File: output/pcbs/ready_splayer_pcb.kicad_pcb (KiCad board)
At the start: 2 copper layers, 124.4 x 92.7 mm, 34 parts

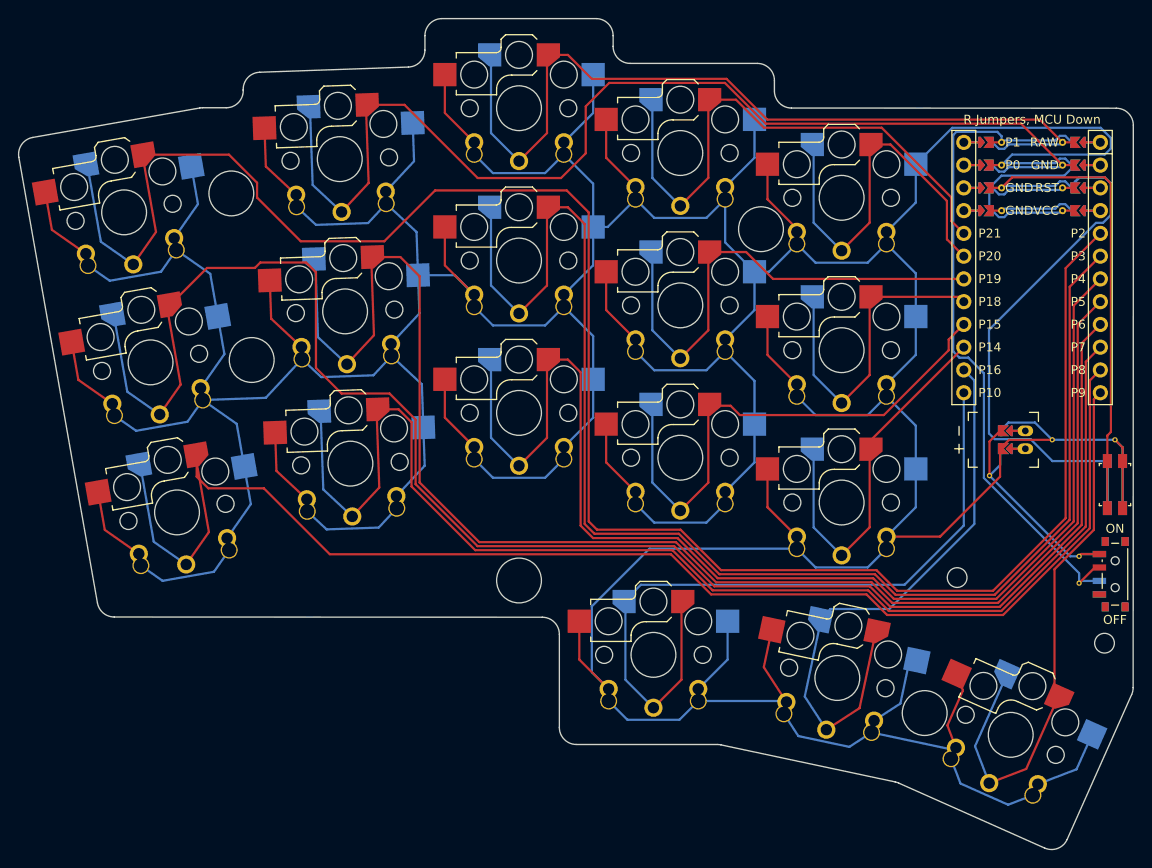
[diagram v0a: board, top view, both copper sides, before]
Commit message: added gerber folder and the final case stl file
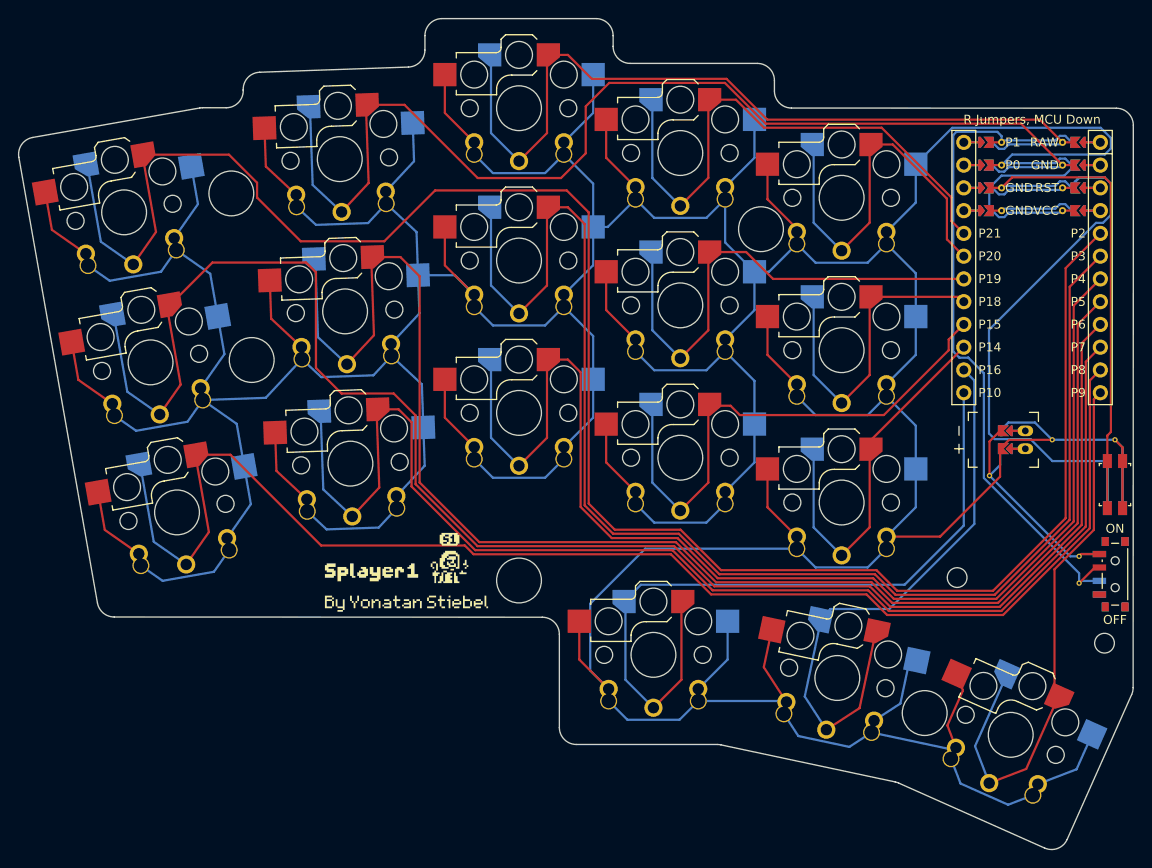
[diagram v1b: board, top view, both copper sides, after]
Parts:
- added G***: LOGO, Logos:splayer1_try2, F.Cu at (117.9, 111.8)
- added G***: LOGO, Logos:splayer1_try2_reverse, F.Cu at (117.7, 111.8)
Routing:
- net P8: track 157.1 -> 155.6 mm
- net P4: track 138.0 -> 136.8 mm
- net P3: track 156.4 -> 155.2 mm
- net P2: track 212.1 -> 210.9 mm
